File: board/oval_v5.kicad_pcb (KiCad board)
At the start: 2 copper layers, 95 x 50 mm, 129 parts, among them J1 HDR-5x1, J10 HDR-4x1, J11 HDR-4x1, J12 HDR-4x1, J13 HDR-4x1, J14 HDR-4x1, J15 HDR-4x1, J16 HDR-4x1, J17 HDR-4x1, J18 Conn_Coaxial, J19 Conn_01x02, J20 Conn_01x02, J22 HDR-2x1, J23 HDR-2x1, J25 Conn_01x06, J3 HDR-4x1, J4 Conn_01x06, J5 Micro_SD_Card, J6 Conn_01x02, J7 HDR-4x1, J8 Conn_01x08, J9 HDR-4x1, P1 USB_C_Plug_USB2.0, Q1 Q_PMOS_GSD, Q2 MMBT3904, Q3 MMBT3904, SW1 SW_DIP_x02, SW2 SW_DIP_x02, U1 RV-8803, U10 SiP32431DR3, U11 SiP32431DR3, U12 SiP32431DR3, U13 SiP32431DR3, U14 SiP32431DR3, U15 PCF8574TS, U16 PCA9548APW, U17 SiP32431DR3, U2 ESP32-S3-WROOM-1, U3 TMP117xxDRV, U4 RFM95W-915S2, U7 MAX3485, U8 AP7361C-33E, U9 AP7361C-33E

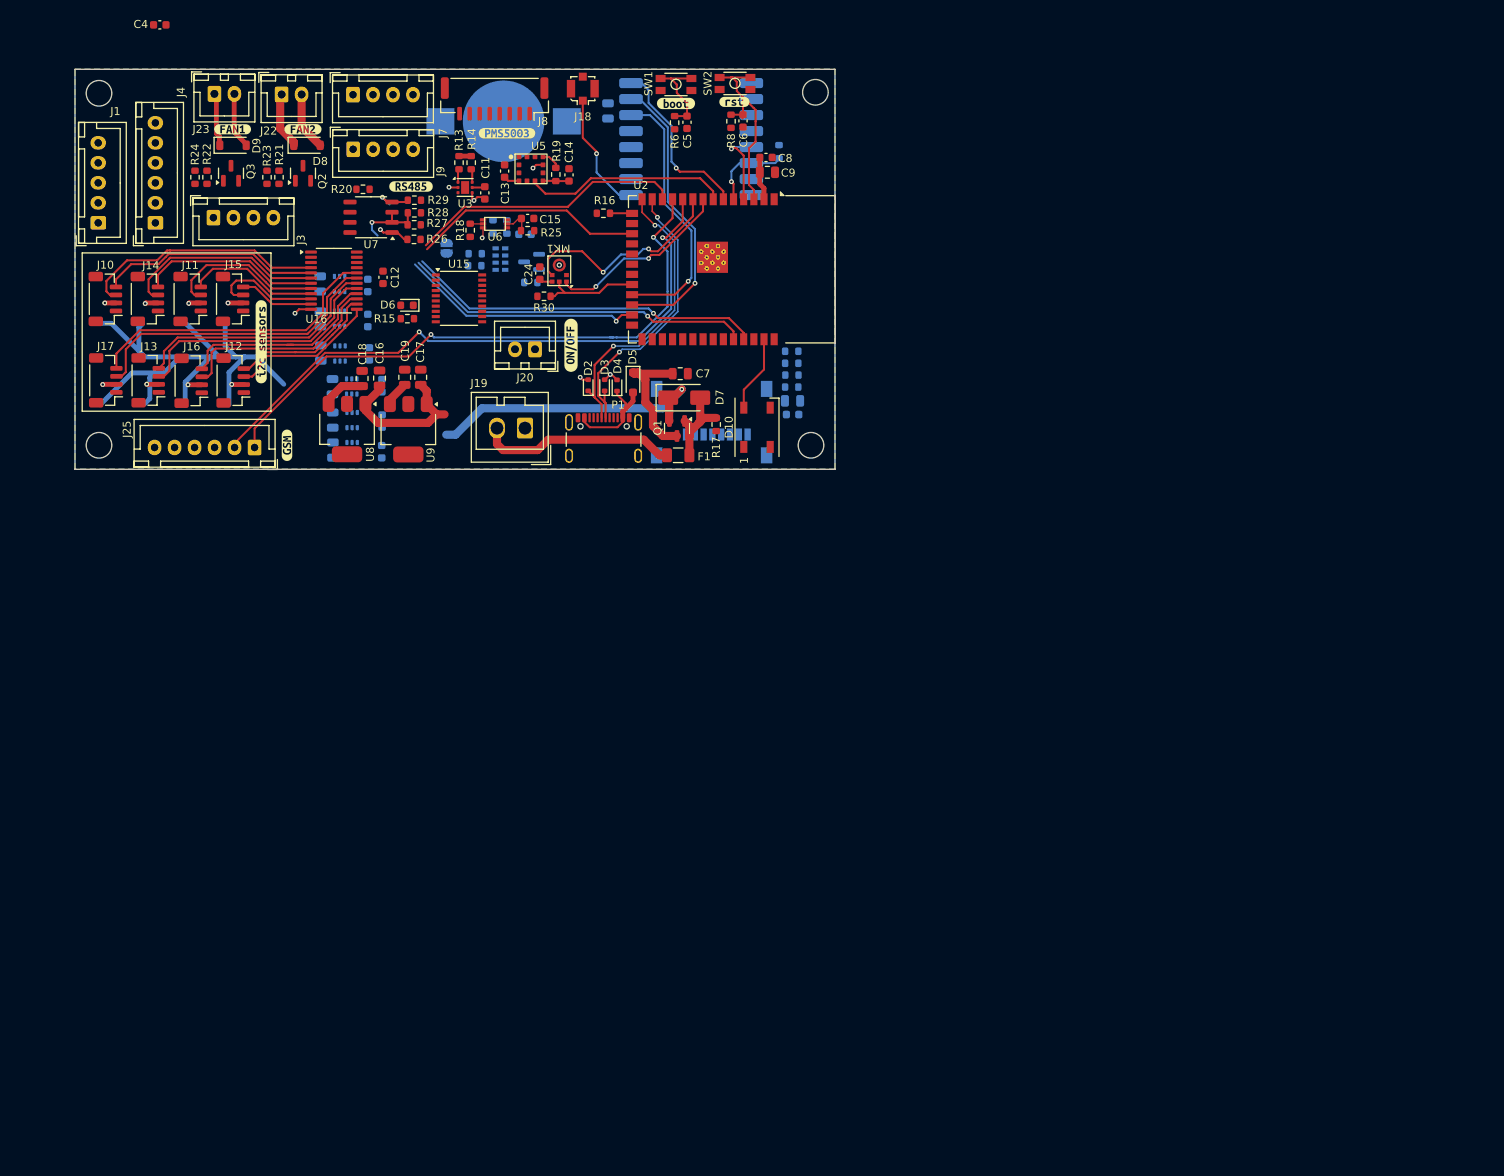
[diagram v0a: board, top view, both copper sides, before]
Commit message: working on layout -  defining connectors and cables
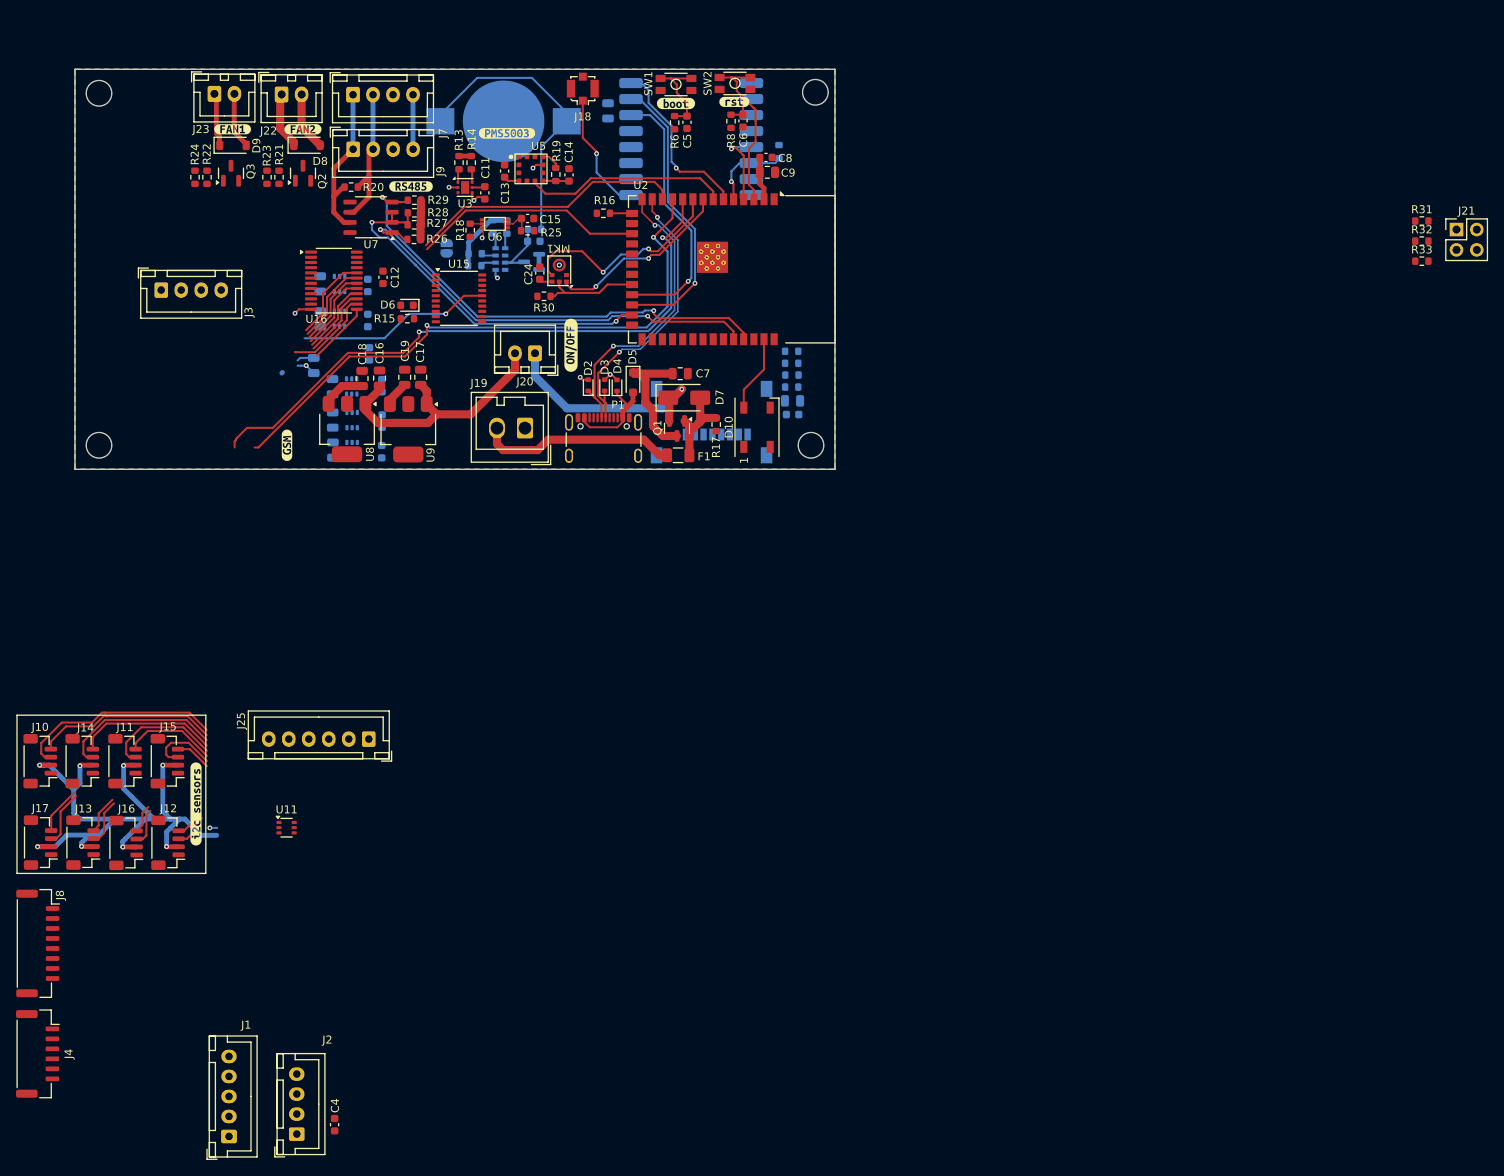
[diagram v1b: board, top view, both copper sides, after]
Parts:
- added J2: HDR-4x1, Connector_JST:JST_XH_B4B-XH-A_1x04_P2.50mm_Vertical, F.Cu at (77.7, 183.1)
- added J21: Conn_02x02_Counter_Clockwise, Connector_PinHeader_2.54mm:PinHeader_2x02_P2.54mm_Vertical, F.Cu at (222.7, 70.0)
- added R31: 10K, Resistor_SMD:R_0603_1608Metric, F.Cu at (218.4, 69.0)
- added R32: 10K, Resistor_SMD:R_0603_1608Metric, F.Cu at (218.4, 71.5)
- added R33: 10K, Resistor_SMD:R_0603_1608Metric, F.Cu at (218.4, 74.0)
- J4: footprint Connector_JST:JST_XH_B6B-XH-A_1x06_P2.50mm_Vertical -> Connector_JST:JST_GH_SM06B-GHS-TB_1x06-1MP_P1.25mm_Horizontal
- U11: moved to F.Cu
- moved C4 139.2 mm to (82.5, 181.9), turned to -90 degrees
- moved J8 120.0 mm to (45.4, 159.3), turned to -90 degrees
- moved J1 115.4 mm to (69.2, 183.4)
- moved J4 104.9 mm to (45.3, 173.1), turned to -90 degrees
- moved U11 59.6 mm to (76.5, 144.8), turned to 0 degrees
- moved J10 58.3 mm to (45.6, 136.5)
- moved J11 58.3 mm to (56.2, 136.5)
- moved J14 58.3 mm to (50.9, 136.5)
- moved J15 58.3 mm to (61.5, 136.5)
- moved J12 58.3 mm to (61.6, 146.7)
- moved J16 58.3 mm to (56.4, 146.7)
- moved kibuzzard-6993384F 58.3 mm to (65.1, 141.8)
- moved J13 58.3 mm to (51.0, 146.7)
- moved J17 58.3 mm to (45.7, 146.7)
- moved J25 39.1 mm to (86.7, 133.7)
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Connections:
- U12 pad 3: V_S3_EN -> V_RF_EN
- U15 pad 11: EN_V_RF -> V_RF_EN
- U15 pad 12: EN_V_DL -> V_DL_EN
- U15 pad 14: EN_V_S1 -> V_S1_EN
- U15 pad 16: EN_V_S2 -> V_S2_EN
- U15 pad 17: EN_V_GSM -> V_GSM_EN
- U15 pad 6: unconnected-(U15-A0-Pad6) -> GND
- U15 pad 7: unconnected-(U15-A1-Pad7) -> GND
- U15 pad 9: unconnected-(U15-A2-Pad9) -> GND
- U16 pad 1: unconnected-(U16-A0-Pad1) -> GND
- U16 pad 2: unconnected-(U16-A1-Pad2) -> GND
- U16 pad 21: unconnected-(U16-A2-Pad21) -> GND
- U16 pad 3: unconnected-(U16-~{RESET}-Pad3) -> Net-(U16-~{RESET})
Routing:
- net Net-(BT1-+): track 0.00 -> 36.2 mm
- net V_S2_EN: track 0.00 -> 24.4 mm, vias 0 -> 1
- net SCL_7: track 37.6 -> 16.8 mm
- net SDA_7: track 38.2 -> 17.4 mm
- net /RS485_B: track 0.68 -> 20.8 mm
- net +5V: track 19.3 -> 39.3 mm
- net /RS485_A: track 0.00 -> 18.2 mm
- net SCL_6: track 31.3 -> 14.9 mm
- net SDA_6: track 32.2 -> 15.7 mm
- net SCL_5: track 25.9 -> 12.8 mm
- net SDA_5: track 25.8 -> 13.6 mm
- net V_DL: track 0.00 -> 10.8 mm
- net RS485_RX: track 49.5 -> 59.1 mm
- net 5V_VDD: track 38.3 -> 30.4 mm
- net Net-(D1-K): track 0.00 -> 7.55 mm
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
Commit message: assignint pines
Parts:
- added C33: 100n, Capacitor_SMD:C_0603_1608Metric, F.Cu at (245.4, 99.5)
- added C34: 10u, Capacitor_SMD:C_0805_2012Metric, F.Cu at (249.6, 109.1)
- added R34: 10k, Resistor_SMD:R_0603_1608Metric, F.Cu at (245.4, 102.0)
- added R35: 10k, Resistor_SMD:R_0603_1608Metric, F.Cu at (245.4, 104.5)
- added R36: 10K, Resistor_SMD:R_0603_1608Metric, F.Cu at (245.4, 107.1)
- added R37: 10K, Resistor_SMD:R_0603_1608Metric, F.Cu at (245.4, 109.6)
- added U18: PCA9555PW, Package_SO:TSSOP-24_4.4x7.8mm_P0.65mm, F.Cu at (252.2, 103.0)
- added kibuzzard-699C8DA6: G***, kibuzzard-699C8DA6, F.Cu at (49.7, 174.0)
- added kibuzzard-699C8DCD: G***, kibuzzard-699C8DCD, F.Cu at (49.9, 159.0)
- J8: footprint Connector_JST:JST_GH_SM08B-GHS-TB_1x08-1MP_P1.25mm_Horizontal -> Connector_Molex:Molex_PicoBlade_53261-0871_1x08-1MP_P1.25mm_Horizontal
- R10, R11: value 2.2k -> 10k
- U11: moved to B.Cu
- moved J25 93.5 mm to (112.0, 43.8)
- moved J5 63.2 mm to (191.7, 105.8)
- moved U4 62.4 mm to (170.7, 103.3)
- moved C2 58.3 mm to (197.9, 95.3), turned to -90 degrees
- moved U2 57.1 mm to (188.9, 68.1)
- moved C3 56.5 mm to (196.1, 95.4), turned to -90 degrees
- moved R5 55.6 mm to (194.2, 95.5), turned to -90 degrees
- moved R4 53.5 mm to (192.7, 95.5), turned to -90 degrees
- moved R3 52.1 mm to (191.2, 95.5), turned to -90 degrees
- moved R2 50.9 mm to (189.8, 95.5), turned to -90 degrees
- moved J3 47.8 mm to (96.8, 109.0)
- moved J1 20.0 mm to (62.2, 164.7)
- moved C4 17.9 mm to (67.0, 172.8)
- moved J2 16.4 mm to (62.0, 178.3)
- moved U11 7.85 mm to (68.6, 144.9)
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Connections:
- J8 pad 1: unconnected-(J8-Pin_1-Pad1) -> +5V
- J8 pad 2: unconnected-(J8-Pin_2-Pad2) -> GND
- J8 pad 3: V_S2 -> PMS_SET
- J8 pad 4: S_TXD -> PMS_Rx
- J8 pad 5: S_RXD -> PMS_Tx
- J8 pad 7: GND -> unconnected-(J8-Pin_7-Pad7)
- J8 pad 8: +5V -> unconnected-(J8-Pin_8-Pad8)
- U2 pad 18: SPI_CS -> SD_CS
- U2 pad 23: rfm_dio0 -> unconnected-(U2-GPIO21-Pad23)
- U2 pad 25: RS485_EN -> rfm_dio2
- U2 pad 31: unconnected-(U2-GPIO38/FSPIWP/SUBSPIWP-Pad31) -> rfm_dio0
- U2 pad 32: unconnected-(U2-MTCK/GPIO39/CLK_OUT3/SUBSPICS1-Pad32) -> rfm_RST
- U2 pad 33: unconnected-(U2-MTDO/GPIO40/CLK_OUT2-Pad33) -> rfm_CS
- U2 pad 34: unconnected-(U2-MTDI/GPIO41/CLK_OUT1-Pad34) -> PMS_Tx
- U2 pad 35: unconnected-(U2-MTMS/GPIO42-Pad35) -> PMS_Rx
- U2 pad 4: rfm_CS -> unconnected-(U2-GPIO4/TOUCH4/ADC1_CH3-Pad4)
- U2 pad 5: rfm_RST -> GSM_RST
- U2 pad 6: rfm_dio2 -> GSM_PWRKEY

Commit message: updateing 27/02
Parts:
- removed U15: PCF8574TS, Package_SO:SSOP-20_4.4x6.5mm_P0.65mm
- D8, D9, Q2, Q3, R21, R22, R23, R24, kibuzzard-6994F00B, kibuzzard-6994F01D: moved to B.Cu
- J1: footprint Connector_JST:JST_XH_B5B-XH-A_1x05_P2.50mm_Vertical -> Connector_JST:JST_PH_B5B-PH-K_1x05_P2.00mm_Vertical
- J10, J11, J12, J13, J14, J15, J16, J17: footprint Connector_JST:JST_SH_BM04B-SRSS-TB_1x04-1MP_P1.00mm_Vertical -> Connector_JST:JST_PH_B4B-PH-K_1x04_P2.00mm_Vertical
- J2, J3: footprint Connector_JST:JST_XH_B4B-XH-A_1x04_P2.50mm_Vertical -> Connector_JST:JST_SH_BM04B-SRSS-TB_1x04-1MP_P1.00mm_Vertical
- J22, J23: footprint Connector_JST:JST_XH_B2B-XH-A_1x02_P2.50mm_Vertical -> Connector_JST:JST_PH_S2B-PH-SM4-TB_1x02-1MP_P2.00mm_Horizontal; moved to B.Cu
- J7, J9: footprint Connector_JST:JST_XH_B4B-XH-A_1x04_P2.50mm_Vertical -> Connector_JST:JST_PH_B4B-PH-K_1x04_P2.00mm_Vertical
- moved C33 180.2 mm to (68.2, 66.6)
- moved C34 180.2 mm to (72.5, 76.2)
- moved R34 180.2 mm to (68.2, 69.1)
- moved R35 180.2 mm to (68.2, 71.6)
- moved R36 180.2 mm to (68.2, 74.1)
- moved R37 180.2 mm to (68.2, 76.6)
- moved U18 180.2 mm to (75.0, 70.0)
- moved J4 139.1 mm to (116.0, 54.0), turned to 180 degrees
- moved kibuzzard-699C8DA6 132.7 mm to (115.0, 58.5), turned to 0 degrees
- moved J2 132.1 mm to (105.5, 53.5), turned to 0 degrees
- moved C9 117.2 mm to (19.5, 56.7)
- moved kibuzzard-69934843 117.2 mm to (15.3, 47.9)
- moved BT1 117.2 mm to (-13.5, 50.3)
- moved C10 117.2 mm to (-0.45, 49.0)
- moved C12 117.2 mm to (-28.6, 69.8)
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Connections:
- U2 pad 23: unconnected-(U2-GPIO21-Pad23) -> V_L_EN
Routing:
- net V_S2: track 82.1 -> 0.11 mm, vias 8 -> 0
- net SDA_0: track 25.8 -> 0.00 mm
- net SCL_0: track 22.7 -> 0.00 mm
- net SDA_1: track 20.5 -> 0.00 mm
- net SCL_1: track 17.6 -> 0.00 mm
- net SDA_2: track 14.9 -> 0.00 mm
- net SCL_2: track 11.6 -> 0.00 mm
- net SDA_3: track 8.79 -> 0.00 mm
- net SDA_7: track 17.4 -> 10.3 mm
- net SCL_7: track 16.8 -> 10.8 mm
- net SDA_6: track 15.7 -> 9.76 mm
- net SCL_6: track 14.9 -> 10.0 mm
- net SDA_5: track 13.6 -> 8.91 mm
- net SCL_3: track 4.51 -> 0.00 mm
- net SDA_4: track 12.3 -> 7.89 mm
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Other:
- board size 95 x 50 mm -> 100 x 60 mm

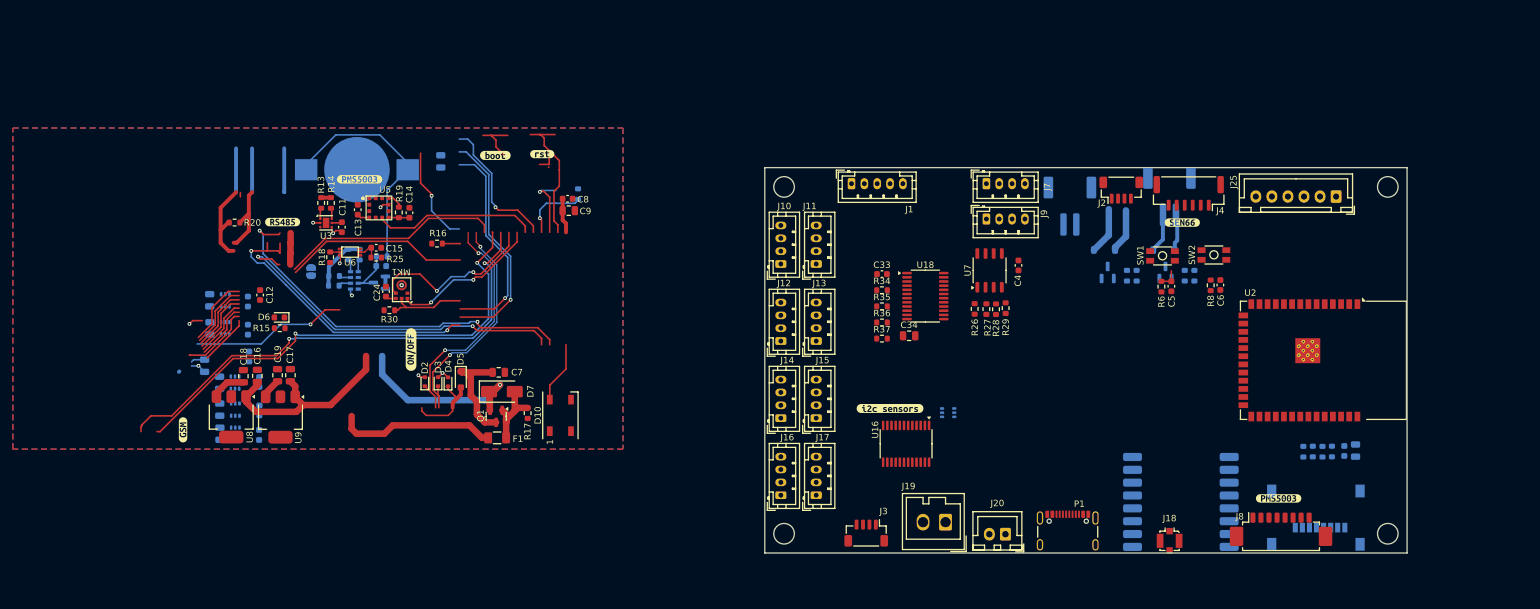
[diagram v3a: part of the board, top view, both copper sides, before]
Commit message: adding layout review
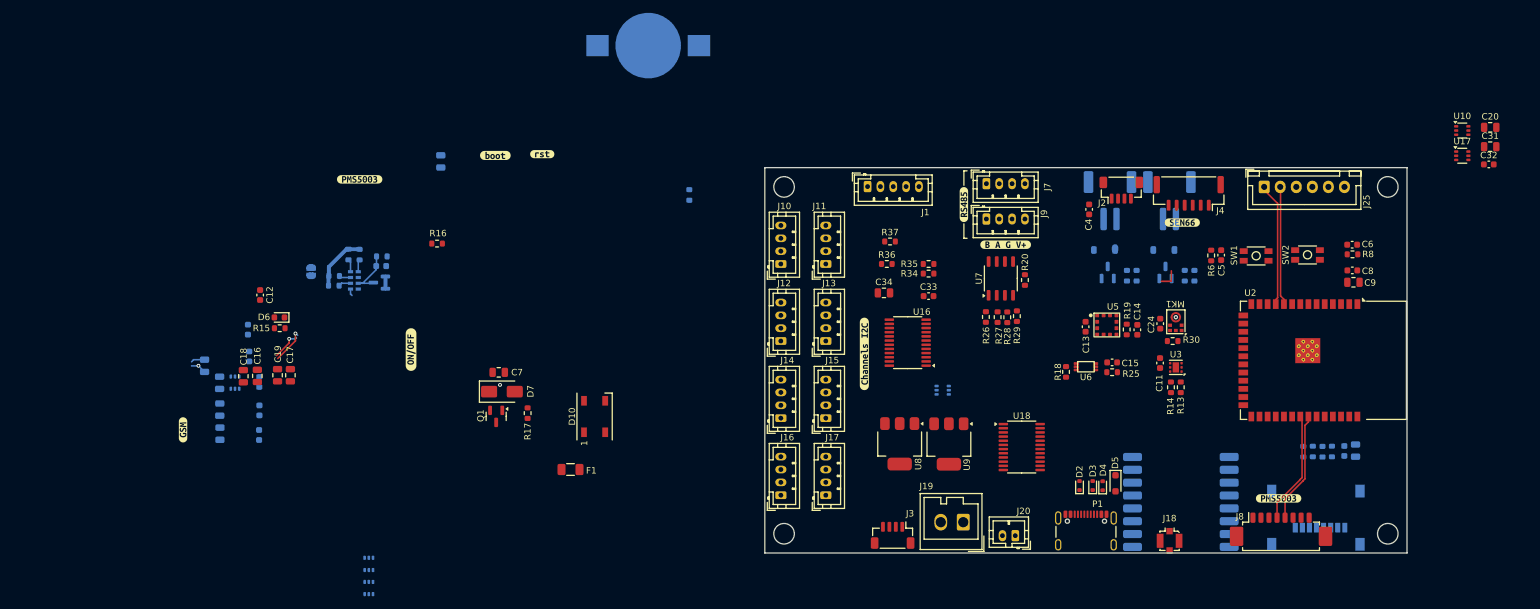
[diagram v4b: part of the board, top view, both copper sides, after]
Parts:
- removed kibuzzard-6993384F: G***, kibuzzard-6993384F
- added kibuzzard-69A86736: G***, kibuzzard-69A86736, F.Cu at (87.5, 62.0)
- added kibuzzard-69A867E5: G***, kibuzzard-69A867E5, F.Cu at (65.5, 79.0)
- C20, C31, C32, U10, U17: moved to F.Cu
- J20: footprint Connector_JST:JST_XH_B2B-XH-A_1x02_P2.50mm_Vertical -> Connector_JST:JST_PH_B2B-PH-K_1x02_P2.00mm_Vertical
- moved C20 201.8 mm to (162.9, 43.7), turned to 0 degrees
- moved C31 200.8 mm to (162.9, 46.7), turned to 0 degrees
- moved U10 195.0 mm to (158.6, 44.2), turned to 0 degrees
- moved C32 194.4 mm to (162.7, 49.5), turned to 0 degrees
- moved U17 193.9 mm to (158.6, 48.1), turned to 0 degrees
- moved R13 136.9 mm to (114.8, 84.2), turned to -90 degrees
- moved U3 134.2 mm to (114.0, 81.1), turned to 180 degrees
- moved R14 133.9 mm to (113.2, 84.2), turned to -90 degrees
- moved C11 129.1 mm to (111.5, 80.4), turned to 90 degrees
- moved R20 123.4 mm to (90.5, 67.5), turned to 90 degrees
- moved C9 122.7 mm to (141.7, 67.8)
- moved C8 122.7 mm to (141.5, 66.0)
- moved R30 122.0 mm to (113.5, 77.0)
- moved C24 120.6 mm to (111.6, 74.3)
- moved MK1 120.6 mm to (114.0, 74.0)
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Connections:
- U2 pad 22: SD_MIC -> MIC_SD
- U2 pad 32: rfm_RST -> GSM_RST
- U2 pad 33: rfm_CS -> PMS_Rx
- U2 pad 35: PMS_Rx -> GSM_PWRKEY
- U2 pad 4: unconnected-(U2-GPIO4/TOUCH4/ADC1_CH3-Pad4) -> rfm_CS
- U2 pad 5: GSM_RST -> rfm_RST
- U2 pad 6: GSM_PWRKEY -> rfm_dio0
- U2 pad 8: WS_MIC -> MIC_WS
- U2 pad 9: SCK_MIC -> MIC_SCK
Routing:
- net RS485_RX: track 59.1 -> 0.00 mm, vias 2 -> 0
- net GSM_Rx: track 78.3 -> 23.2 mm, vias 2 -> 1
- net RS485_TX: track 55.0 -> 0.00 mm, vias 2 -> 0
- net GSM_Tx: track 75.0 -> 24.7 mm, vias 2 -> 1
- net RS485_EN: track 46.7 -> 0.00 mm, vias 2 -> 0
- net +5V: track 39.3 -> 0.00 mm
- net USB_D+: track 36.8 -> 0.00 mm, vias 2 -> 0
- net Net-(BT1-+): track 36.2 -> 0.00 mm
- net SDA: track 38.0 -> 1.92 mm
- net USB_D-: track 36.0 -> 0.00 mm, vias 2 -> 0
- net rfm_dio1: track 36.0 -> 0.00 mm, vias 1 -> 0
- net rfm_dio0: track 33.2 -> 0.00 mm, vias 1 -> 0
- net SCL: track 32.5 -> 1.99 mm
- net 5V_VDD: track 30.4 -> 0.16 mm
- net SCK_MIC: track 27.1 -> 0.00 mm, vias 2 -> 0
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- removed copper zone on B.Cu, net GND
- removed copper zone on F.Cu, net GND
